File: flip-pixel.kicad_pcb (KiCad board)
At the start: 2 copper layers, 157.5 x 129.5 mm, 182 parts, among them J1 Barrel-Jack, Q1 DMN62D0U-7, Q10 STS8DN6LF6AG, Q11 DMN62D0U-7, Q12 DMN62D0U-7, Q13 STS8DN6LF6AG, Q14 DMN62D0U-7, Q15 DMN62D0U-7, Q16 STS8DN6LF6AG, Q17 DMN62D0U-7, Q18 DMN62D0U-7, Q19 STS8DN6LF6AG, Q2 DMN62D0U-7, Q20 DMN62D0U-7, Q21 DMN62D0U-7, Q22 STS8DN6LF6AG, Q23 DMN62D0U-7, Q24 DMN62D0U-7, Q25 STS8DN6LF6AG, Q26 DMN62D0U-7, Q27 DMN62D0U-7, Q28 STS8DN6LF6AG, Q29 DMN62D0U-7, Q3 DMN62D0U-7, Q30 DMN62D0U-7, Q31 STS8DN6LF6AG, Q4 STS8DN6LF6AG, Q5 DMN62D0U-7, Q6 DMN62D0U-7, Q7 STS8DN6LF6AG, Q8 DMN62D0U-7, Q9 DMN62D0U-7, U1 LM2665M6, U2 ESP32_DevBoard, U3 ACS722

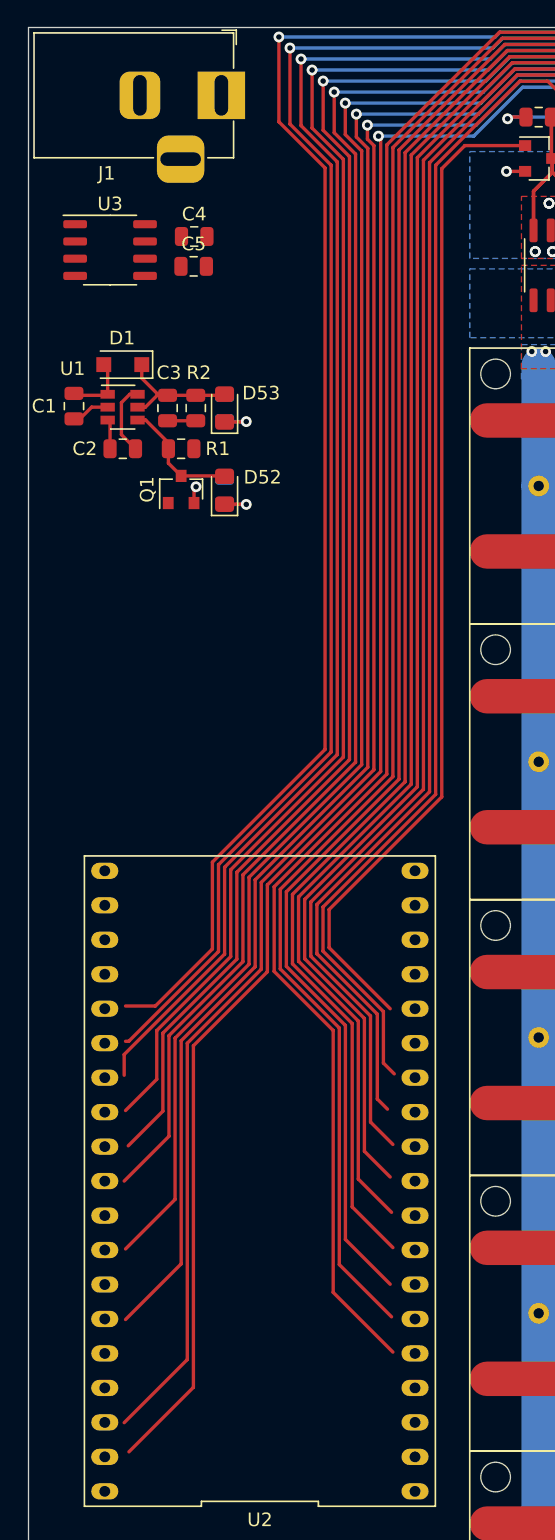
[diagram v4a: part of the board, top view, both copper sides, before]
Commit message: Updated Pins to match routes
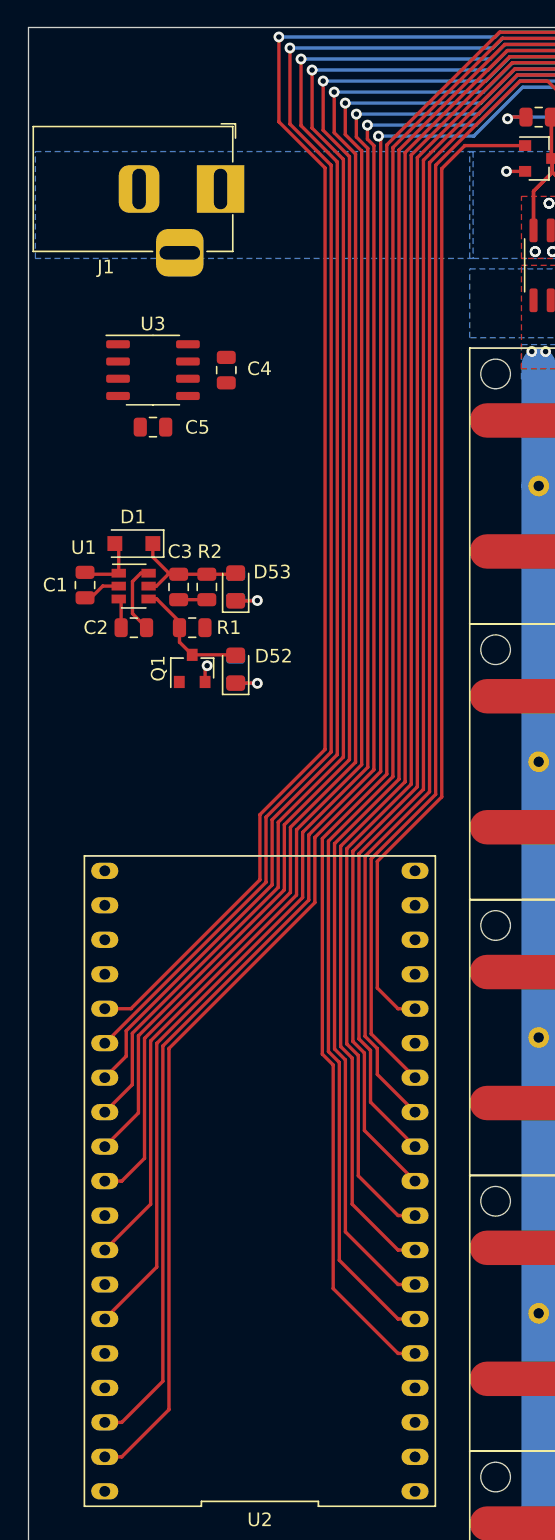
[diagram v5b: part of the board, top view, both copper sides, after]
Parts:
- moved D52 13.2 mm to (110.5, 72.7)
- moved R23 13.2 mm to (110.5, 72.7)
- moved U1 13.2 mm to (103.0, 66.6)
- moved C1 13.2 mm to (99.4, 66.5)
- moved C2 13.2 mm to (103.0, 69.6)
- moved C3 13.2 mm to (106.3, 66.6)
- moved D1 13.2 mm to (103.0, 63.4)
- moved D53 13.2 mm to (110.5, 66.6)
- moved Q1 13.2 mm to (107.3, 72.6)
- moved R1 13.2 mm to (107.3, 69.6)
- moved R2 13.2 mm to (108.4, 66.6)
- moved R24 13.2 mm to (110.5, 66.6)
- moved C5 12.2 mm to (104.4, 54.8)
- moved C4 10.1 mm to (109.8, 50.6), turned to 270 degrees
- moved U3 9.39 mm to (104.4, 50.6)
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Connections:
- net Net-(J1-Pad1) renamed /Power_Input
- Q12 pad 1: /Row4/Low_ct -> /Row4L
- Q15 pad 1: /Row5/Low_ct -> /Row5L
- Q18 pad 1: /Column2/Low_ct -> /Col2L
- Q21 pad 1: /Column1/Low_ct -> /Col1L
- Q24 pad 1: /Column3/Low_ct -> /Col3L
- Q27 pad 1: /Column4/Low_ct -> /Col4L
- Q3 pad 1: /Row2/Low_ct -> /Row2L
- Q30 pad 1: /Column5/Low_ct -> /Col5L
- Q6 pad 1: /Row1/Low_ct -> /Row1L
- Q9 pad 1: /Row3/Low_ct -> /Row3L
- U2 pad 10: /Row3L -> /Col3L
- U2 pad 11: /Row4H -> /Col2H
- U2 pad 12: /Row4L -> /Col2L
- U2 pad 13: /Row5H -> /Col1H
- U2 pad 15: /Row5L -> /Col1L
- U2 pad 24: /Col5L -> /Row5H
- U2 pad 25: /Col5H -> /Row5L
- U2 pad 26: /Col4L -> /Row4H
- U2 pad 27: /Col4H -> /Row4L
- U2 pad 28: /Col3L -> /Row3H
- U2 pad 29: /Col3H -> /Row3L
- U2 pad 31: /Col2L -> /Row2H
- U2 pad 33: /Col2H -> /Row2L
- U2 pad 36: /Col1L -> /Row1H
- U2 pad 37: /Col1H -> /Row1L
- U2 pad 5: /Row1H -> /Col5H
- U2 pad 6: /Row1L -> /Col5L
- U2 pad 7: /Row2H -> /Col4H
- U2 pad 8: /Row2L -> /Col4L
- U2 pad 9: /Row3H -> /Col3H
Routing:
- net /Row5L: track 0.00 -> 331.7 mm, vias 0 -> 2
- net /Row5/Low_ct: track 331.1 -> 0.00 mm, vias 2 -> 0
- net /Row4L: track 0.00 -> 310.7 mm, vias 0 -> 2
- net /Row4/Low_ct: track 310.0 -> 0.00 mm, vias 2 -> 0
- net /Row3L: track 0.00 -> 290.6 mm, vias 0 -> 2
- net /Row3/Low_ct: track 289.3 -> 0.00 mm, vias 2 -> 0
- net /Row2L: track 0.00 -> 274.0 mm, vias 0 -> 2
- net /Row2/Low_ct: track 273.4 -> 0.00 mm, vias 2 -> 0
- net /Row1L: track 0.00 -> 258.9 mm, vias 0 -> 2
- net /Row1/Low_ct: track 257.0 -> 0.00 mm, vias 2 -> 0
- net /Column5/Low_ct: track 190.6 -> 0.00 mm
- net /Col5L: track 0.00 -> 189.3 mm
- net /Column4/Low_ct: track 163.0 -> 0.00 mm
- net /Col4L: track 0.00 -> 161.6 mm
- net /Column3/Low_ct: track 135.2 -> 0.00 mm
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
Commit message: All traces routed
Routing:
- net /current: track 0.00 -> 86.5 mm, vias 0 -> 1
- net +5V: track 4.52 -> 60.1 mm, vias 20 -> 29
- net +10V: track 262.7 -> 313.1 mm, vias 22 -> 25
- net /enable: track 0.00 -> 23.8 mm
- net GND: track 47.6 -> 63.0 mm, vias 74 -> 77
- net /Row5/Low: track 100.3 -> 104.8 mm
- net /Row4/Low: track 100.3 -> 104.8 mm
- net /Row3/High: track 105.2 -> 109.6 mm
- net /Row2/Low: track 100.1 -> 104.5 mm
- net /Row5/High: track 104.9 -> 109.3 mm
- net /Row4/High: track 104.6 -> 109.1 mm
- net /Row3/Low: track 100.1 -> 104.5 mm
- net /Row2/High: track 105.2 -> 109.6 mm
- net /Row1/Low: track 101.2 -> 104.8 mm
- net /Row1/High: track 104.8 -> 108.3 mm
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- added copper zone on F.Cu, net /Power_Input

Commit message: Updated All Traces
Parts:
- added JP1: BypassJumper, Jumper:SolderJumper-2_P1.3mm_Open_RoundedPad1.0x1.5mm, F.Cu at (62.0, 50.4)
- U3: value ACS722 -> INA250A3; footprint Custom-Footprints:SO-8_3.9x4.9mm_P1.27mm -> Package_SO:TSSOP-16_4.4x5mm_P0.65mm
- moved D10 44.3 mm to (101.3, 140.5)
- moved D11 44.3 mm to (101.3, 145.5)
- moved D12 44.3 mm to (121.7, 59.2)
- moved D13 44.3 mm to (121.7, 64.3)
- moved D14 44.3 mm to (121.7, 79.5)
- moved D15 44.3 mm to (121.7, 84.6)
- moved D16 44.3 mm to (121.7, 99.8)
- moved D17 44.3 mm to (121.7, 104.9)
- moved D18 44.3 mm to (121.7, 120.1)
- moved D19 44.3 mm to (121.7, 125.2)
- moved D2 44.3 mm to (101.3, 59.2)
- moved D20 44.3 mm to (121.7, 140.5)
- moved D21 44.3 mm to (121.7, 145.5)
- moved D22 44.3 mm to (142.0, 59.2)
- moved D23 44.3 mm to (142.0, 64.3)
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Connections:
- C4 pad 1: +5V -> /Power_Input
- D10 pad 1: Net-(D10-Pad1) -> Net-(D2-Pad1)
- D10 pad 2: /Row5/High -> /Row1/High
- D11 pad 1: /Row5/Low -> /Row1/Low
- D11 pad 2: Net-(D10-Pad1) -> Net-(D2-Pad1)
- D12 pad 1: Net-(D12-Pad1) -> Net-(D2-Pad1)
- D13 pad 2: Net-(D12-Pad1) -> Net-(D2-Pad1)
- D14 pad 1: Net-(D14-Pad1) -> Net-(D2-Pad1)
- D14 pad 2: /Row2/High -> /Row1/High
- D15 pad 1: /Row2/Low -> /Row1/Low
- D15 pad 2: Net-(D14-Pad1) -> Net-(D2-Pad1)
- D16 pad 1: Net-(D16-Pad1) -> Net-(D2-Pad1)
- D16 pad 2: /Row3/High -> /Row1/High
- D17 pad 1: /Row3/Low -> /Row1/Low
- D17 pad 2: Net-(D16-Pad1) -> Net-(D2-Pad1)
- D18 pad 1: Net-(D18-Pad1) -> Net-(D2-Pad1)
- D18 pad 2: /Row4/High -> /Row1/High
- D19 pad 1: /Row4/Low -> /Row1/Low
- D19 pad 2: Net-(D18-Pad1) -> Net-(D2-Pad1)
- D20 pad 1: Net-(D20-Pad1) -> Net-(D2-Pad1)
- D20 pad 2: /Row5/High -> /Row1/High
- D21 pad 1: /Row5/Low -> /Row1/Low
- D21 pad 2: Net-(D20-Pad1) -> Net-(D2-Pad1)
- D22 pad 1: Net-(D22-Pad1) -> Net-(D2-Pad1)
- D23 pad 2: Net-(D22-Pad1) -> Net-(D2-Pad1)
- D24 pad 1: Net-(D24-Pad1) -> Net-(D2-Pad1)
- D24 pad 2: /Row2/High -> /Row1/High
- D25 pad 1: /Row2/Low -> /Row1/Low
- D25 pad 2: Net-(D24-Pad1) -> Net-(D2-Pad1)
- D26 pad 1: Net-(D26-Pad1) -> Net-(D2-Pad1)
- D26 pad 2: /Row3/High -> /Row1/High
- D27 pad 1: /Row3/Low -> /Row1/Low
- D27 pad 2: Net-(D26-Pad1) -> Net-(D2-Pad1)
- D28 pad 1: Net-(D28-Pad1) -> Net-(D2-Pad1)
- D28 pad 2: /Row4/High -> /Row1/High
- D29 pad 1: /Row4/Low -> /Row1/Low
- D29 pad 2: Net-(D28-Pad1) -> Net-(D2-Pad1)
- D30 pad 1: Net-(D30-Pad1) -> Net-(D2-Pad1)
- D30 pad 2: /Row5/High -> /Row1/High
- D31 pad 1: /Row5/Low -> /Row1/Low
- D31 pad 2: Net-(D30-Pad1) -> Net-(D2-Pad1)
- D32 pad 1: Net-(D32-Pad1) -> Net-(D2-Pad1)
- D33 pad 2: Net-(D32-Pad1) -> Net-(D2-Pad1)
- D34 pad 1: Net-(D34-Pad1) -> Net-(D2-Pad1)
- D34 pad 2: /Row2/High -> /Row1/High
- D35 pad 1: /Row2/Low -> /Row1/Low
- D35 pad 2: Net-(D34-Pad1) -> Net-(D2-Pad1)
- D36 pad 1: Net-(D36-Pad1) -> Net-(D2-Pad1)
- D36 pad 2: /Row3/High -> /Row1/High
- D37 pad 1: /Row3/Low -> /Row1/Low
- D37 pad 2: Net-(D36-Pad1) -> Net-(D2-Pad1)
- D38 pad 1: Net-(D38-Pad1) -> Net-(D2-Pad1)
- D38 pad 2: /Row4/High -> /Row1/High
- D39 pad 1: /Row4/Low -> /Row1/Low
- D39 pad 2: Net-(D38-Pad1) -> Net-(D2-Pad1)
- D4 pad 1: Net-(D4-Pad1) -> Net-(D2-Pad1)
- D4 pad 2: /Row2/High -> /Row1/High
- D40 pad 1: Net-(D40-Pad1) -> Net-(D2-Pad1)
- D40 pad 2: /Row5/High -> /Row1/High
- D41 pad 1: /Row5/Low -> /Row1/Low
- D41 pad 2: Net-(D40-Pad1) -> Net-(D2-Pad1)
- D42 pad 1: Net-(D42-Pad1) -> Net-(D2-Pad1)
- D43 pad 2: Net-(D42-Pad1) -> Net-(D2-Pad1)
- D44 pad 1: Net-(D44-Pad1) -> Net-(D2-Pad1)
- D44 pad 2: /Row2/High -> /Row1/High
- D45 pad 1: /Row2/Low -> /Row1/Low
- D45 pad 2: Net-(D44-Pad1) -> Net-(D2-Pad1)
- D46 pad 1: Net-(D46-Pad1) -> Net-(D2-Pad1)
- D46 pad 2: /Row3/High -> /Row1/High
- D47 pad 1: /Row3/Low -> /Row1/Low
- D47 pad 2: Net-(D46-Pad1) -> Net-(D2-Pad1)
- D48 pad 1: Net-(D48-Pad1) -> Net-(D2-Pad1)
- D48 pad 2: /Row4/High -> /Row1/High
- D49 pad 1: /Row4/Low -> /Row1/Low
- D49 pad 2: Net-(D48-Pad1) -> Net-(D2-Pad1)
- D5 pad 1: /Row2/Low -> /Row1/Low
- D5 pad 2: Net-(D4-Pad1) -> Net-(D2-Pad1)
- D50 pad 1: Net-(D50-Pad1) -> Net-(D2-Pad1)
- D50 pad 2: /Row5/High -> /Row1/High
- D51 pad 1: /Row5/Low -> /Row1/Low
- D51 pad 2: Net-(D50-Pad1) -> Net-(D2-Pad1)
- D6 pad 1: Net-(D6-Pad1) -> Net-(D2-Pad1)
- D6 pad 2: /Row3/High -> /Row1/High
- D7 pad 1: /Row3/Low -> /Row1/Low
- D7 pad 2: Net-(D6-Pad1) -> Net-(D2-Pad1)
- D8 pad 1: Net-(D8-Pad1) -> Net-(D2-Pad1)
- D8 pad 2: /Row4/High -> /Row1/High
- D9 pad 1: /Row4/Low -> /Row1/Low
- D9 pad 2: Net-(D8-Pad1) -> Net-(D2-Pad1)
- U3 pad 1: /Power_Input -> +5V
- U3 pad 2: /Power_Input -> +5V
- U3 pad 4: +5V -> Net-(U3-Pad4)
- U3 pad 5: GND -> Net-(U3-Pad4)
- U3 pad 7: /current -> GND
- U3 pad 8: +5V -> GND
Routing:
- net /Row1/High: track 108.3 -> 545.9 mm, vias 5 -> 25
- net /Row1/Low: track 104.8 -> 523.3 mm, vias 5 -> 25
- net Net-(D2-Pad1): track 4.82 -> 120.5 mm
- net /Row3/High: track 109.6 -> 0.00 mm, vias 5 -> 0
- net /Row2/High: track 109.6 -> 0.00 mm, vias 5 -> 0
- net /Row5/High: track 109.3 -> 0.00 mm, vias 5 -> 0
- net /Row4/High: track 109.1 -> 0.00 mm, vias 5 -> 0
- net /Row5/Low: track 104.8 -> 0.00 mm, vias 5 -> 0
- net /Row4/Low: track 104.8 -> 0.00 mm, vias 5 -> 0
- net /Row2/Low: track 104.5 -> 0.00 mm, vias 5 -> 0
- net /Row3/Low: track 104.5 -> 0.00 mm, vias 5 -> 0
- net +5V: track 60.1 -> 17.5 mm, vias 29 -> 28
- net /PixelMatrix/Col_5: track 89.3 -> 102.0 mm
- net /PixelMatrix/Col_2: track 90.2 -> 102.9 mm
- net /PixelMatrix/Col_1: track 90.2 -> 102.9 mm
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
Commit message: Logos and SilkScreen
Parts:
- added LOGO1: Logo_Open_Hardware_Small, Symbol:OSHW-Logo2_9.8x8mm_SilkScreen, F.Cu at (62.1, 144.4)
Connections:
- D10 pad 1: Net-(D2-Pad1) -> Net-(D10-Pad1)
- D10 pad 2: /Row1/High -> /Row5/High
- D11 pad 1: /Row1/Low -> /Row5/Low
- D11 pad 2: Net-(D2-Pad1) -> Net-(D10-Pad1)
- D12 pad 1: Net-(D2-Pad1) -> Net-(D12-Pad1)
- D13 pad 2: Net-(D2-Pad1) -> Net-(D12-Pad1)
- D14 pad 1: Net-(D2-Pad1) -> Net-(D14-Pad1)
- D14 pad 2: /Row1/High -> /Row2/High
- D15 pad 1: /Row1/Low -> /Row2/Low
- D15 pad 2: Net-(D2-Pad1) -> Net-(D14-Pad1)
- D16 pad 1: Net-(D2-Pad1) -> Net-(D16-Pad1)
- D16 pad 2: /Row1/High -> /Row3/High
- D17 pad 1: /Row1/Low -> /Row3/Low
- D17 pad 2: Net-(D2-Pad1) -> Net-(D16-Pad1)
- D18 pad 1: Net-(D2-Pad1) -> Net-(D18-Pad1)
- D18 pad 2: /Row1/High -> /Row4/High
- D19 pad 1: /Row1/Low -> /Row4/Low
- D19 pad 2: Net-(D2-Pad1) -> Net-(D18-Pad1)
- D20 pad 1: Net-(D2-Pad1) -> Net-(D20-Pad1)
- D20 pad 2: /Row1/High -> /Row5/High
- D21 pad 1: /Row1/Low -> /Row5/Low
- D21 pad 2: Net-(D2-Pad1) -> Net-(D20-Pad1)
- D22 pad 1: Net-(D2-Pad1) -> Net-(D22-Pad1)
- D23 pad 2: Net-(D2-Pad1) -> Net-(D22-Pad1)
- D24 pad 1: Net-(D2-Pad1) -> Net-(D24-Pad1)
- D24 pad 2: /Row1/High -> /Row2/High
- D25 pad 1: /Row1/Low -> /Row2/Low
- D25 pad 2: Net-(D2-Pad1) -> Net-(D24-Pad1)
- D26 pad 1: Net-(D2-Pad1) -> Net-(D26-Pad1)
- D26 pad 2: /Row1/High -> /Row3/High
- D27 pad 1: /Row1/Low -> /Row3/Low
- D27 pad 2: Net-(D2-Pad1) -> Net-(D26-Pad1)
- D28 pad 1: Net-(D2-Pad1) -> Net-(D28-Pad1)
- D28 pad 2: /Row1/High -> /Row4/High
- D29 pad 1: /Row1/Low -> /Row4/Low
- D29 pad 2: Net-(D2-Pad1) -> Net-(D28-Pad1)
- D30 pad 1: Net-(D2-Pad1) -> Net-(D30-Pad1)
- D30 pad 2: /Row1/High -> /Row5/High
- D31 pad 1: /Row1/Low -> /Row5/Low
- D31 pad 2: Net-(D2-Pad1) -> Net-(D30-Pad1)
- D32 pad 1: Net-(D2-Pad1) -> Net-(D32-Pad1)
- D33 pad 2: Net-(D2-Pad1) -> Net-(D32-Pad1)
- D34 pad 1: Net-(D2-Pad1) -> Net-(D34-Pad1)
- D34 pad 2: /Row1/High -> /Row2/High
- D35 pad 1: /Row1/Low -> /Row2/Low
- D35 pad 2: Net-(D2-Pad1) -> Net-(D34-Pad1)
- D36 pad 1: Net-(D2-Pad1) -> Net-(D36-Pad1)
- D36 pad 2: /Row1/High -> /Row3/High
- D37 pad 1: /Row1/Low -> /Row3/Low
- D37 pad 2: Net-(D2-Pad1) -> Net-(D36-Pad1)
- D38 pad 1: Net-(D2-Pad1) -> Net-(D38-Pad1)
- D38 pad 2: /Row1/High -> /Row4/High
- D39 pad 1: /Row1/Low -> /Row4/Low
- D39 pad 2: Net-(D2-Pad1) -> Net-(D38-Pad1)
- D4 pad 1: Net-(D2-Pad1) -> Net-(D4-Pad1)
- D4 pad 2: /Row1/High -> /Row2/High
- D40 pad 1: Net-(D2-Pad1) -> Net-(D40-Pad1)
- D40 pad 2: /Row1/High -> /Row5/High
- D41 pad 1: /Row1/Low -> /Row5/Low
- D41 pad 2: Net-(D2-Pad1) -> Net-(D40-Pad1)
- D42 pad 1: Net-(D2-Pad1) -> Net-(D42-Pad1)
- D43 pad 2: Net-(D2-Pad1) -> Net-(D42-Pad1)
- D44 pad 1: Net-(D2-Pad1) -> Net-(D44-Pad1)
- D44 pad 2: /Row1/High -> /Row2/High
- D45 pad 1: /Row1/Low -> /Row2/Low
- D45 pad 2: Net-(D2-Pad1) -> Net-(D44-Pad1)
- D46 pad 1: Net-(D2-Pad1) -> Net-(D46-Pad1)
- D46 pad 2: /Row1/High -> /Row3/High
- D47 pad 1: /Row1/Low -> /Row3/Low
- D47 pad 2: Net-(D2-Pad1) -> Net-(D46-Pad1)
- D48 pad 1: Net-(D2-Pad1) -> Net-(D48-Pad1)
- D48 pad 2: /Row1/High -> /Row4/High
- D49 pad 1: /Row1/Low -> /Row4/Low
- D49 pad 2: Net-(D2-Pad1) -> Net-(D48-Pad1)
- D5 pad 1: /Row1/Low -> /Row2/Low
- D5 pad 2: Net-(D2-Pad1) -> Net-(D4-Pad1)
- D50 pad 1: Net-(D2-Pad1) -> Net-(D50-Pad1)
- D50 pad 2: /Row1/High -> /Row5/High
- D51 pad 1: /Row1/Low -> /Row5/Low
- D51 pad 2: Net-(D2-Pad1) -> Net-(D50-Pad1)
- D6 pad 1: Net-(D2-Pad1) -> Net-(D6-Pad1)
- D6 pad 2: /Row1/High -> /Row3/High
- D7 pad 1: /Row1/Low -> /Row3/Low
- D7 pad 2: Net-(D2-Pad1) -> Net-(D6-Pad1)
- D8 pad 1: Net-(D2-Pad1) -> Net-(D8-Pad1)
- D8 pad 2: /Row1/High -> /Row4/High
- D9 pad 1: /Row1/Low -> /Row4/Low
- D9 pad 2: Net-(D2-Pad1) -> Net-(D8-Pad1)
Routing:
- net /Row1/High: track 545.9 -> 108.3 mm, vias 25 -> 5
- net /Row1/Low: track 523.3 -> 104.8 mm, vias 25 -> 5
- net Net-(D2-Pad1): track 120.5 -> 4.82 mm
- net /Row2/High: track 0.00 -> 109.6 mm, vias 0 -> 5
- net /Row3/High: track 0.00 -> 109.6 mm, vias 0 -> 5
- net /Row5/High: track 0.00 -> 109.3 mm, vias 0 -> 5
- net /Row4/High: track 0.00 -> 109.1 mm, vias 0 -> 5
- net /Row5/Low: track 0.00 -> 104.8 mm, vias 0 -> 5
- net /Row4/Low: track 0.00 -> 104.8 mm, vias 0 -> 5
- net /Row3/Low: track 0.00 -> 104.5 mm, vias 0 -> 5
- net /Row2/Low: track 0.00 -> 104.5 mm, vias 0 -> 5
- net /current: track 81.4 -> 86.6 mm
- net Net-(D30-Pad1): track 0.00 -> 4.82 mm
- net Net-(D28-Pad1): track 0.00 -> 4.82 mm
- net Net-(D26-Pad1): track 0.00 -> 4.82 mm
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- added copper zone on F.Cu, net (none)
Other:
- board text added: "Connor Winiarczyk"
- board text added: "Designed By:"
- board text added: "Flip Pixel Display Evaluation Board Spin 1"
- board text added: "https://github.com/Hayden-and-Connor/flip-pixel"
